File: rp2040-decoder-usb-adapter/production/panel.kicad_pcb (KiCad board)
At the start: 2 copper layers, 70 x 70 mm, 276 parts, among them J1 505070-2422, J2 SWD, J3 SPEAKER, J4 MISC1, J8 RAIL_PADS, P1 USB_C_Receptacle_USB2.0_16P

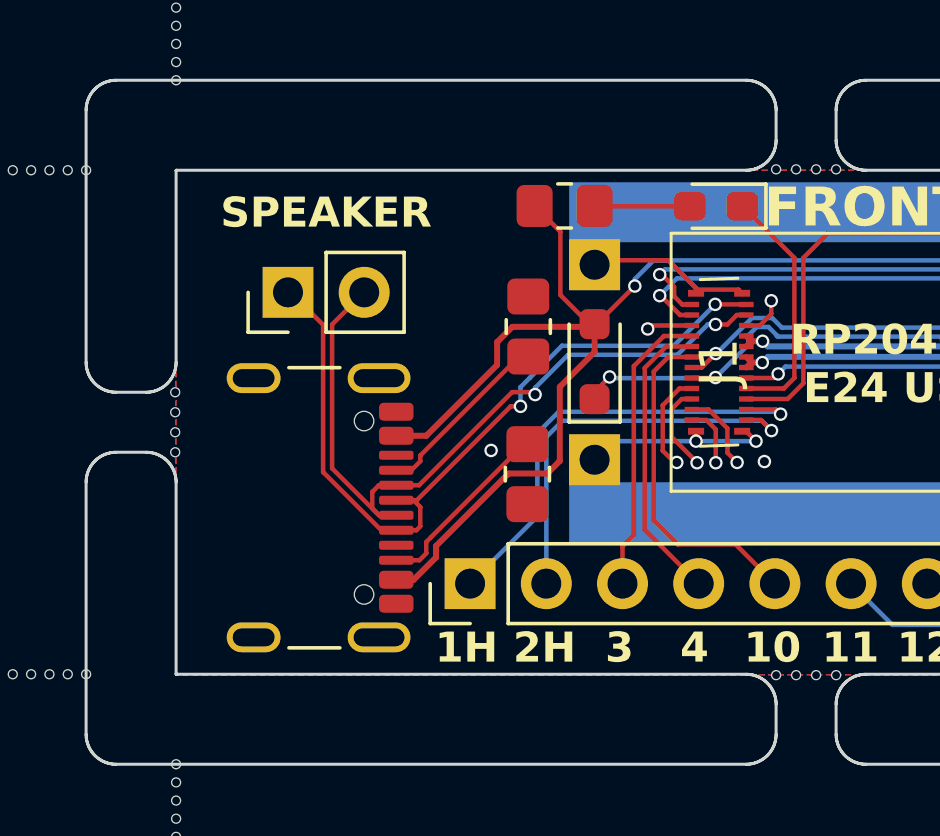
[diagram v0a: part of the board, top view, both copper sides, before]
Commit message: feat: add external capacitor support
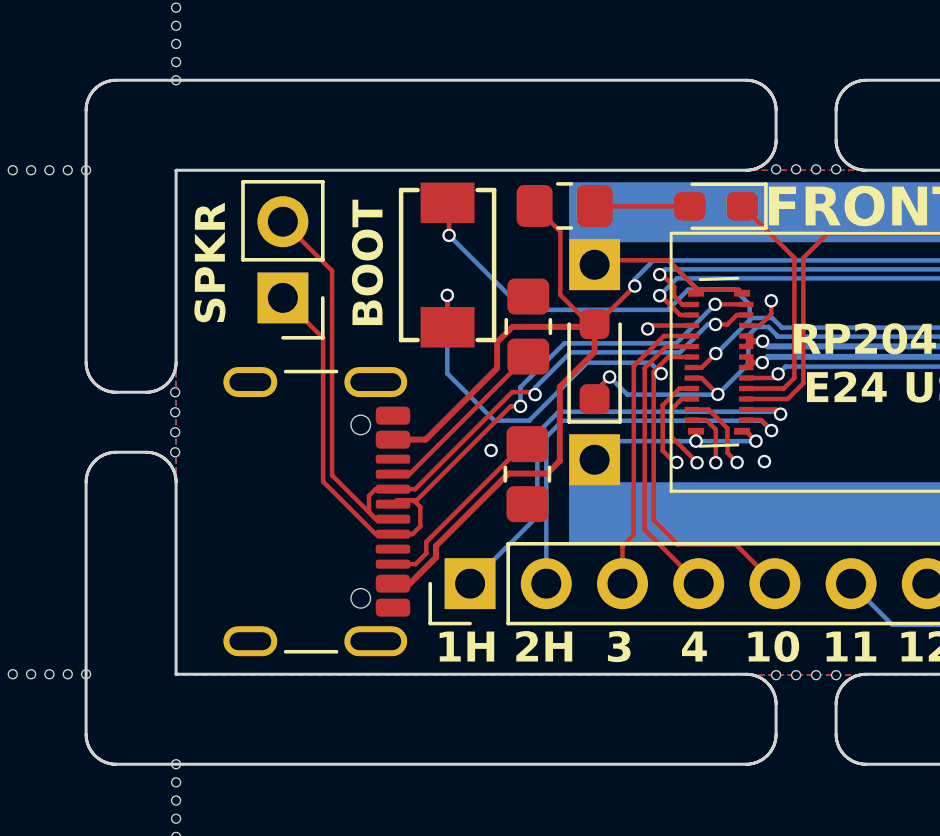
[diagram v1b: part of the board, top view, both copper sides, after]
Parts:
- added SW1: BOOT, Local Library:Xunpu_TS-1088-AR02016, F.Cu at (136.6, 49.8)
- moved J3 0.25 mm to (131.1, 50.9), turned to 180 degrees
- moved P1 0.17 mm to (131.1, 58.0)
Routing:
- net Board_0-VCC: track 27.7 -> 40.9 mm, vias 2 -> 3
- net Board_0-/AUX10: track 11.3 -> 23.8 mm, vias 0 -> 2
- net Board_0-/D-: track 25.7 -> 28.5 mm
- net Board_0-VDC: track 29.3 -> 30.3 mm
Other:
- board text added: "BOOT"
- board text added: "SPKR"
- board text removed: "SPEAKER"

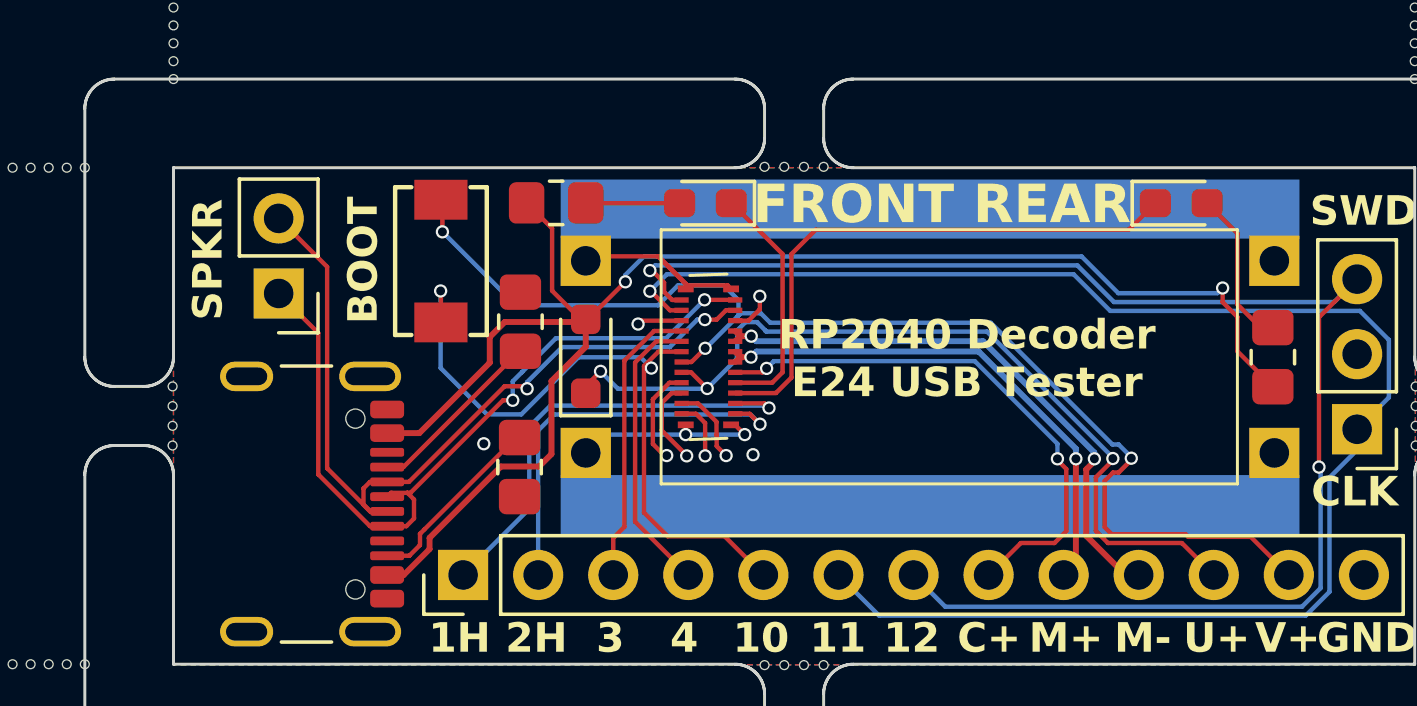
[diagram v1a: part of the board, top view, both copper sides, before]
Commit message: fix: make boot button easier to press
fix: dfm fixes
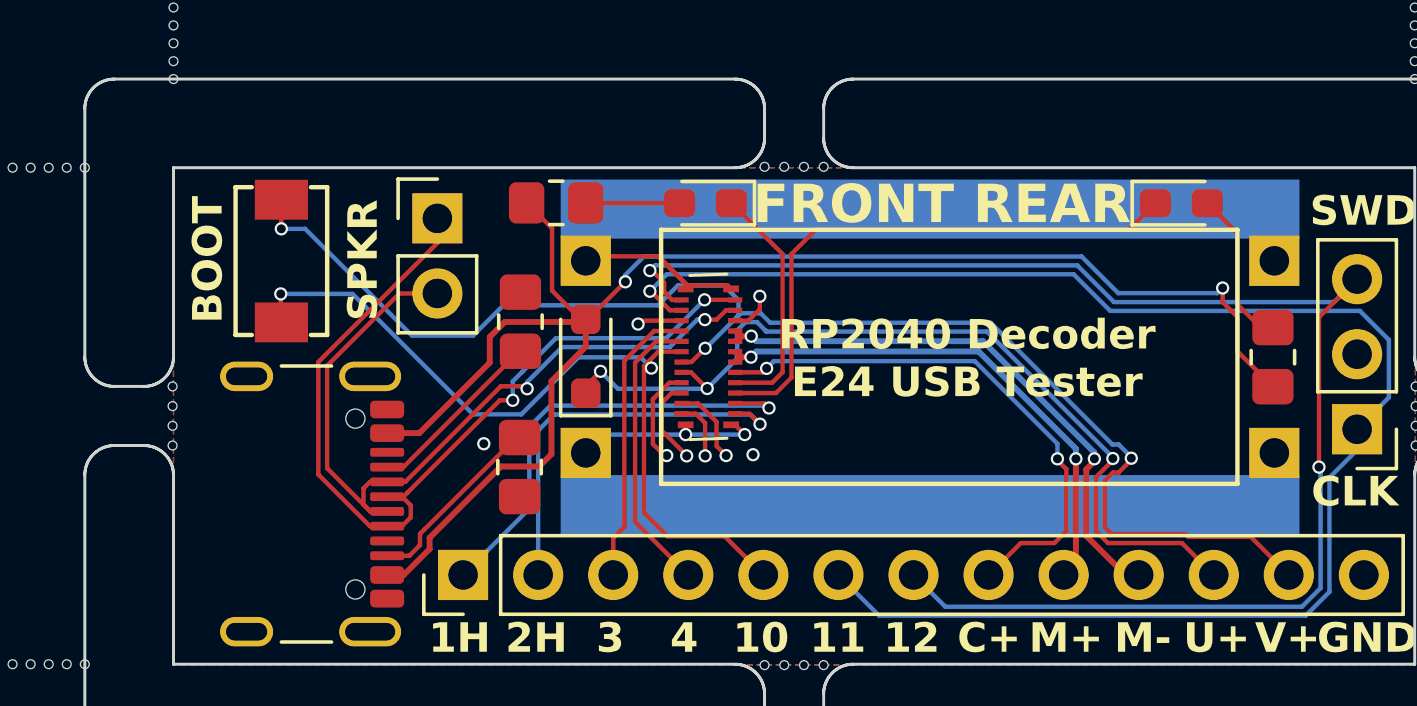
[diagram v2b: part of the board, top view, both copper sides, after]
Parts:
- moved J3 5.94 mm to (136.4, 48.3), turned to 0 degrees
- moved SW1 5.40 mm to (131.2, 49.8)
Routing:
- net Board_0-VCC: track 40.9 -> 47.1 mm
- net Board_0-/D+: track 26.6 -> 30.6 mm
- net Board_0-/AUX10: track 23.8 -> 27.5 mm
- net Board_0-/D-: track 28.5 -> 27.6 mm

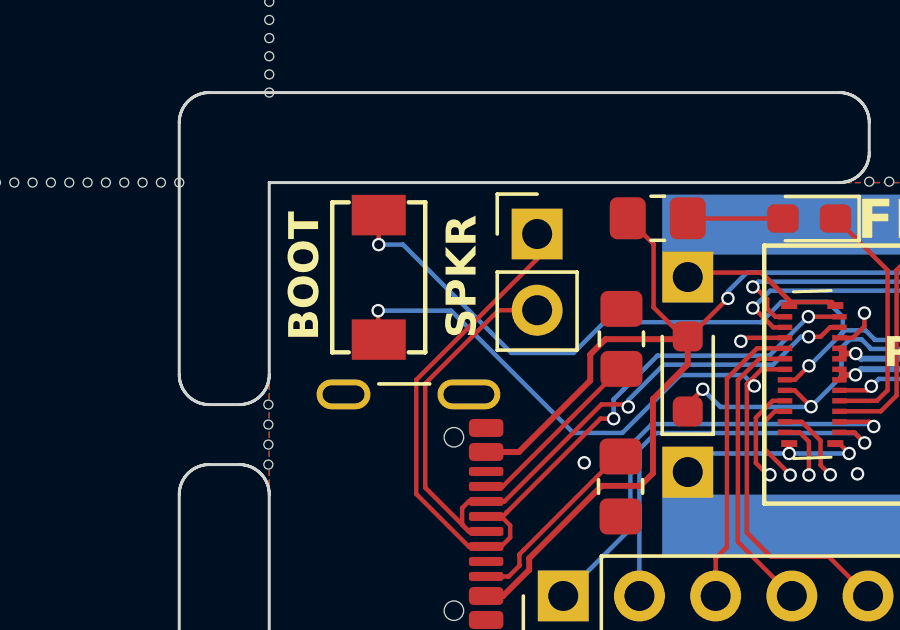
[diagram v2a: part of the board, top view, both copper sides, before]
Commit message: fix: switch button type
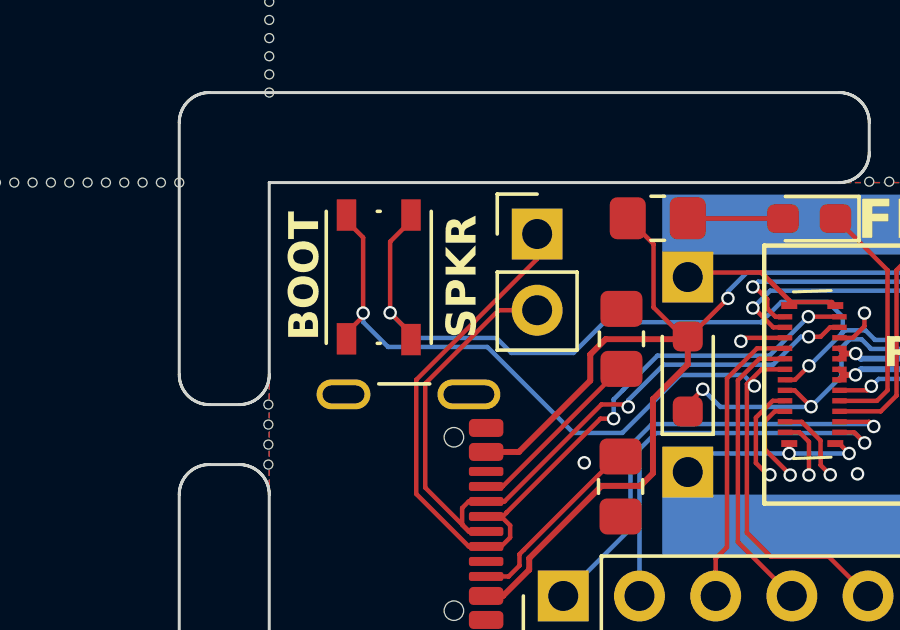
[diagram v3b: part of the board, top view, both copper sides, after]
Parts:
- SW1: footprint Local Library:Xunpu_TS-1088-AR02016 -> Button_Switch_SMD:SW_Push_1P1T_NO_Vertical_Wuerth_434133025816
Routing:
- net Board_0-/AUX10: track 27.5 -> 31.8 mm
- net Board_0-VCC: track 47.1 -> 49.5 mm
